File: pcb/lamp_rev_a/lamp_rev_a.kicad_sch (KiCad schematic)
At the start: 0 parts

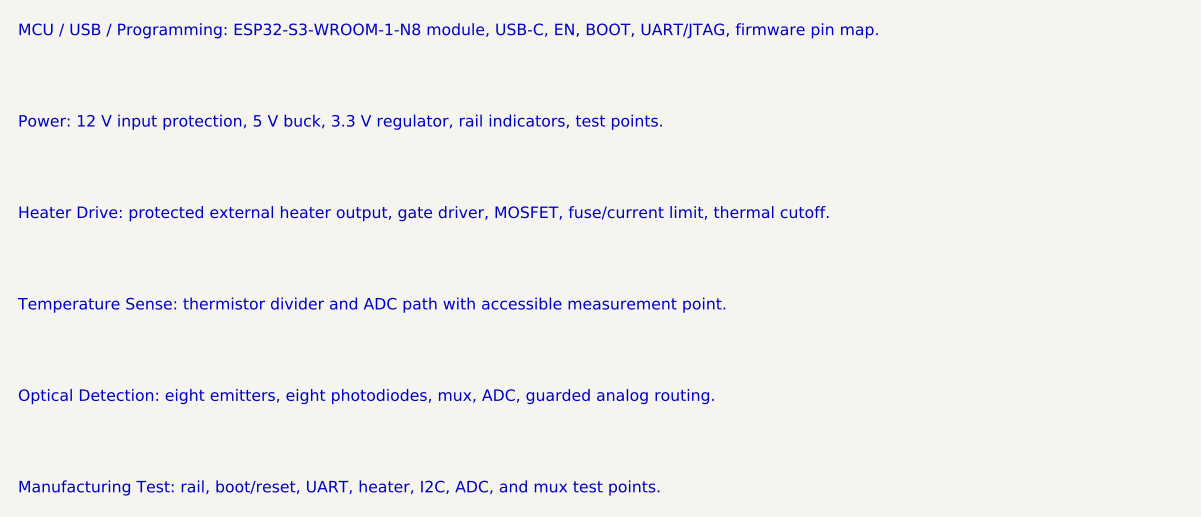
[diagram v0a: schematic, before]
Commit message: Lock LAMP Rev A placement contract
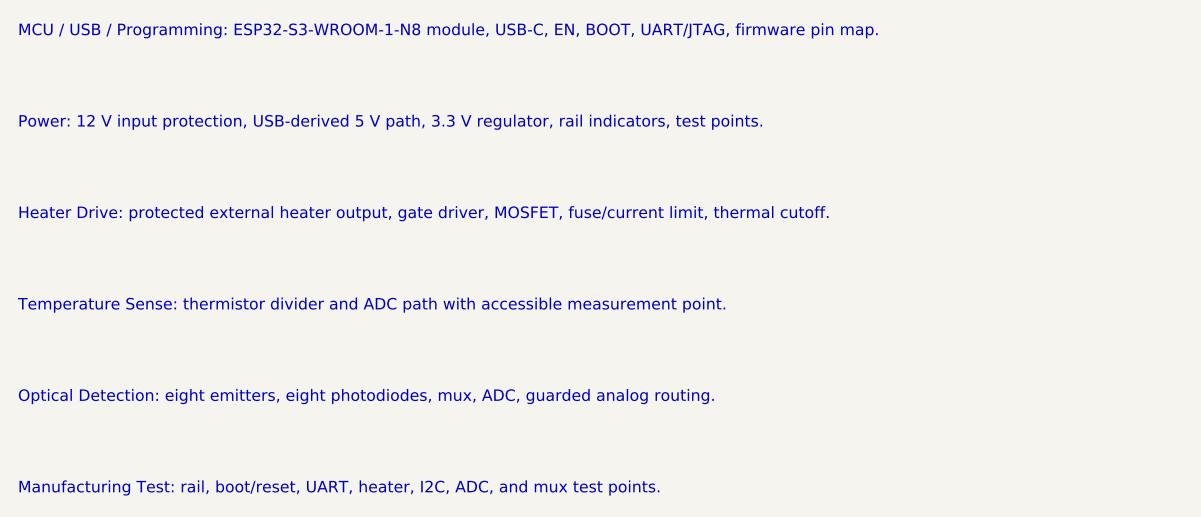
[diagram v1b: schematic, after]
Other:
- note added: "Power: 12 V input protection, USB-derived 5 V path, 3.3 V regulator, rail indicators, test points."
- note removed: "Power: 12 V input protection, 5 V buck, 3.3 V regulator, rail indicators, test points."
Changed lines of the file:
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@@
     (effects (font (size 1.27 1.27)) (justify left))
   )
-  (text "Power: 12 V input protection, 5 V buck, 3.3 V regulator, rail indicators, test points."
+  (text "Power: 12 V input protection, USB-derived 5 V path, 3.3 V regulator, rail indicators, test points."
     (at 20.32 35.56 0)
     (effects (font (size 1.27 1.27)) (justify left))
